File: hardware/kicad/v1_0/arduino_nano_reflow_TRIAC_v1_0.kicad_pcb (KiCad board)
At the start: 2 copper layers, 100 x 50 mm, 34 parts, among them J1 AC IN 220v, J10 CONN_01X17, J11 CONN_01X03, J12 MOUNTING_HOLE, J13 MOUNTING_HOLE, J14 MOUNTING_HOLE, J15 MOUNTING_HOLE, J2 HEATER, J3 DC IN 12V, J4 12v FAN, J5 CONN_01X03, J6 CONN_01X03, J7 CONN_01X03, J8 CONN_01X03, J9 CONN_01X05, Q1 IRF540N, U1 MOC3020M

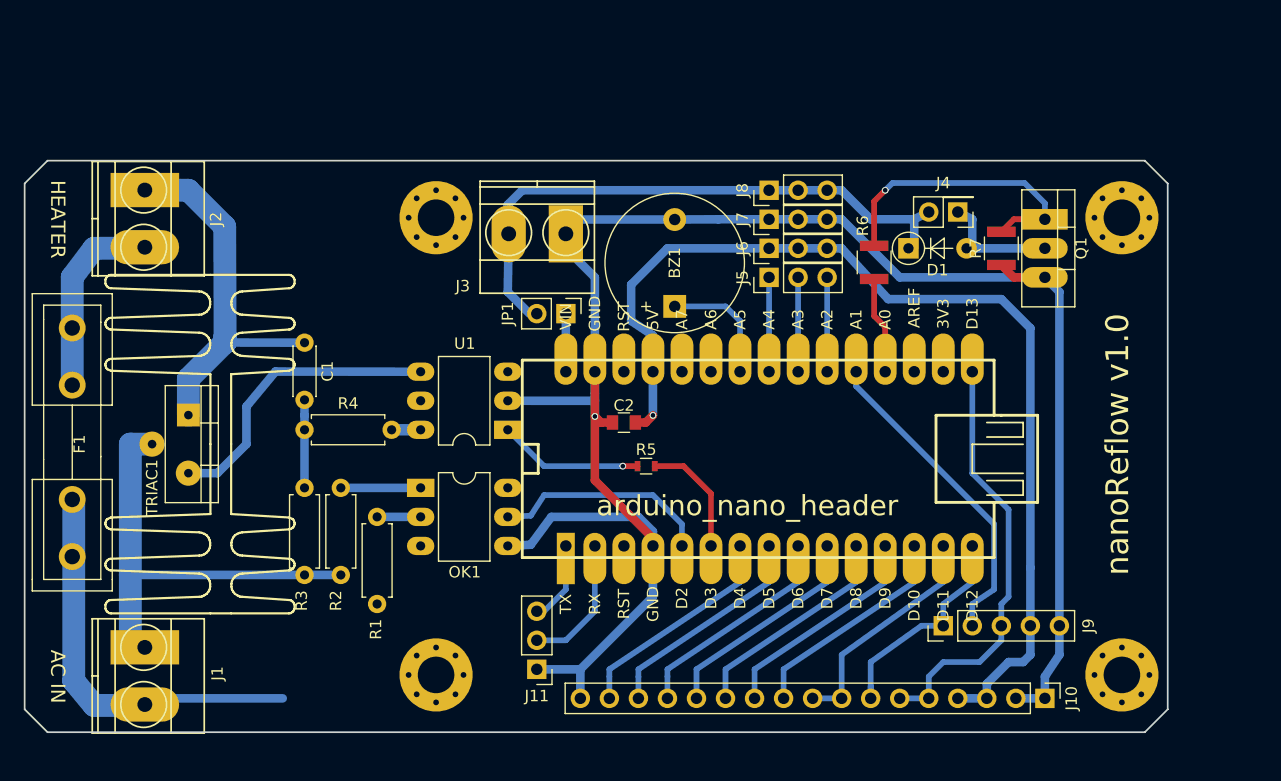
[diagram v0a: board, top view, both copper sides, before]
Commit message: - new revision of board - suitable for production with oshpark - updated footprints - cross checked with original schematics
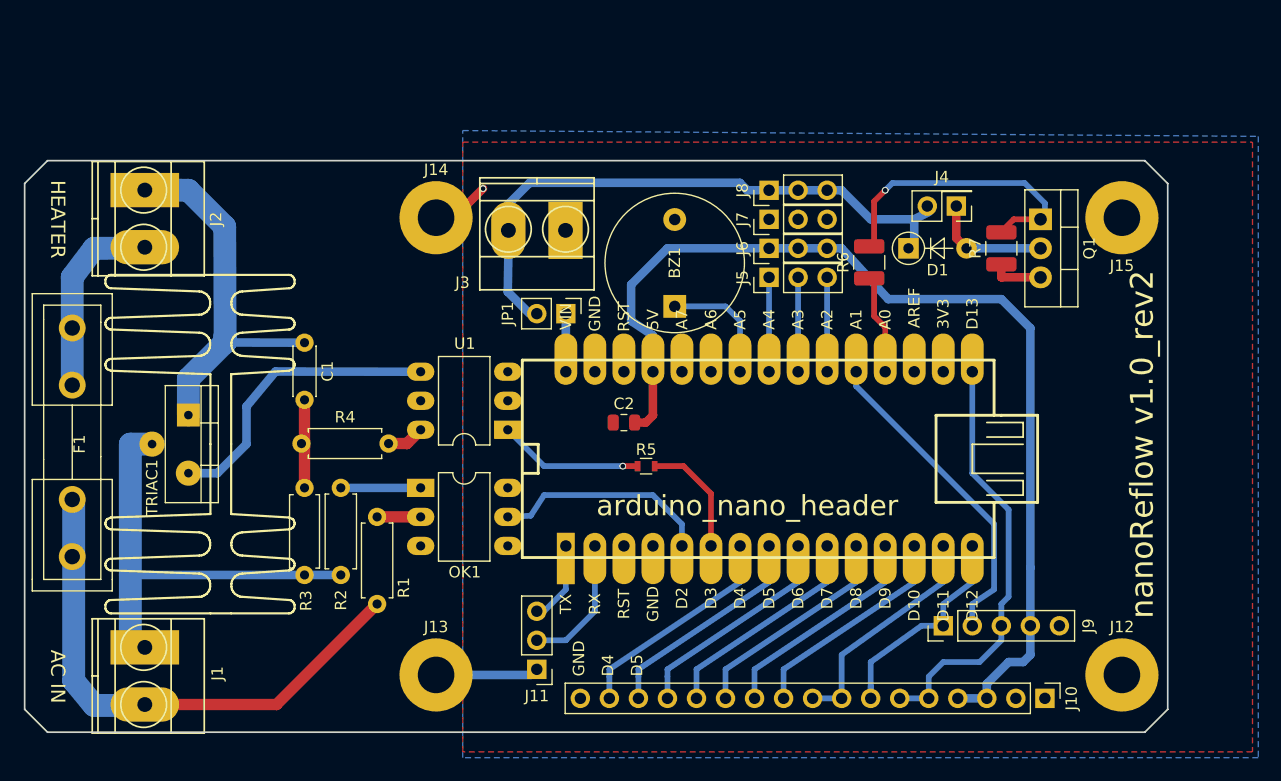
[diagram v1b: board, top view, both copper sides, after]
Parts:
- BZ1: footprint Buzzers_Beepers:Buzzer_12x9.5RM7.6 -> Buzzer_Beeper:Buzzer_12x9.5RM7.6
- C2: footprint Capacitors_SMD:C_0805 -> Capacitor_SMD:C_0805_2012Metric
- J12, J13, J14, J15: footprint Mounting_Holes:MountingHole_3.2mm_M3_Pad_Via -> MountingHole:MountingHole_3.2mm_M3_Pad
- Q1: footprint TO_SOT_Packages_THT:TO-220_Vertical -> Package_TO_SOT_THT:TO-220-3_Vertical
- R1, R2: footprint Resistors_THT:R_Axial_DIN0207_L6.3mm_D2.5mm_P7.62mm_Horizontal -> Resistor_THT:R_Axial_DIN0207_L6.3mm_D2.5mm_P7.62mm_Horizontal
- R6, R7: footprint Resistors_SMD:R_1210 -> Resistor_SMD:R_1210_3225Metric
- moved R4 1.23 mm to (124.7, 92.7)
- moved J4 0.54 mm to (182.0, 72.0)
- moved R6 0.43 mm to (174.4, 76.9)
- moved Q1 0.38 mm to (189.4, 73.1)
- moved J3 0.30 mm to (147.8, 74.1)
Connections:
- J12 pad 1: Net-(J12-Pad1) -> GND
- J13 pad 1: Net-(J13-Pad1) -> GND
- J14 pad 1: Net-(J14-Pad1) -> GND
- J15 pad 1: Net-(J15-Pad1) -> GND
- R1 pad 1: (no net) -> AC2_IN
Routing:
- net GND: track 169.1 -> 18.7 mm
- net AC2_IN: track 34.9 -> 46.7 mm
- net /AC_CAP: track 7.06 -> 7.92 mm
- net /MOC_AC1: track 2.54 -> 3.31 mm
- net /OC2: track 3.18 -> 3.81 mm
- net 12v: track 51.4 -> 51.9 mm
- net 5V: track 90.9 -> 90.8 mm, vias 1 -> 0
- added copper zone on B.Cu, net GND
- added copper zone on F.Cu, net GND
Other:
- board text added: "D4"
- board text added: "D5"
- board text added: "GND"
- board text added: "nanoReflow v1.0_rev2"
- board text removed: "nanoReflow v1.0"

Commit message: update footprint to match kicad 5.1.6 - SIP suitable for oshpark
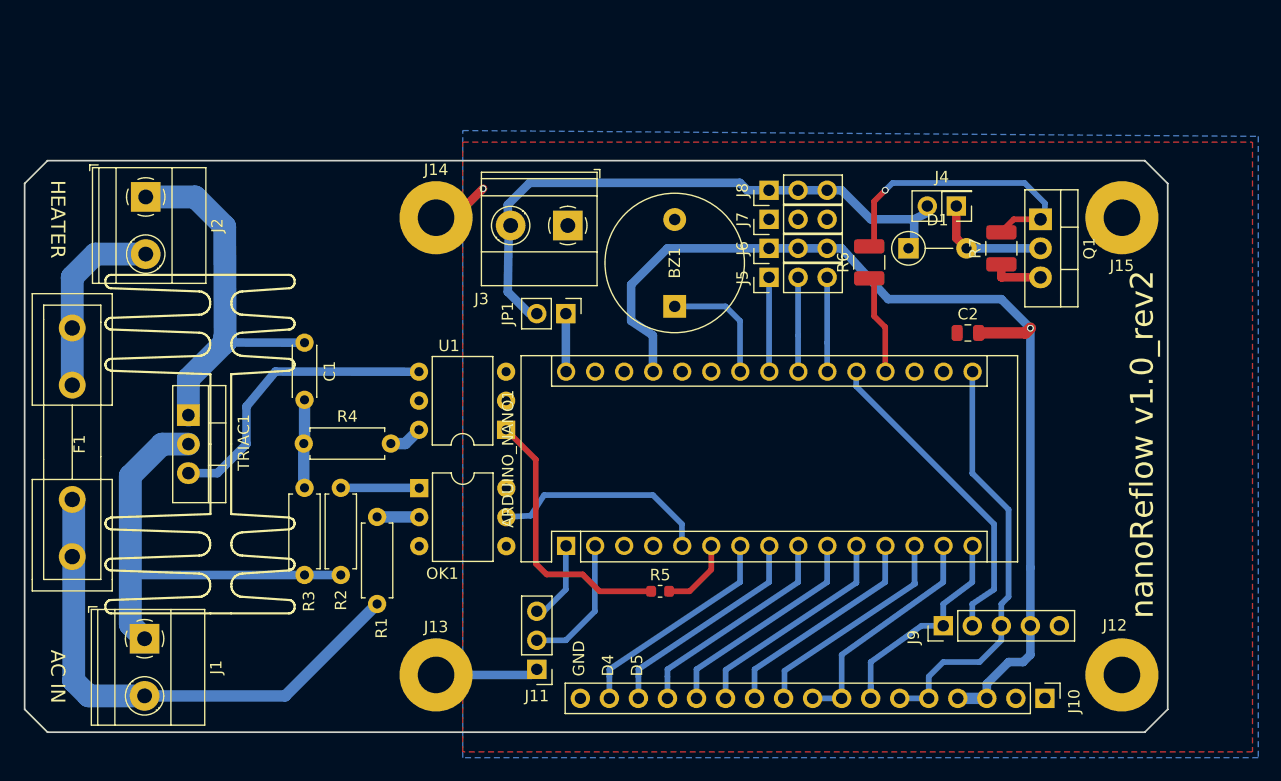
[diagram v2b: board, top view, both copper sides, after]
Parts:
- ARDUINO_NANO1: footprint local_modules:arduino_nano_header -> Module:Arduino_Nano
- C1: footprint Capacitors_THT:C_Disc_D4.3mm_W1.9mm_P5.00mm -> Capacitor_THT:C_Disc_D4.3mm_W1.9mm_P5.00mm
- D1: footprint Diodes_THT:D_A-405_P5.08mm_Vertical_AnodeUp -> Diode_THT:D_A-405_P5.08mm_Vertical_AnodeUp
- J1, J2, J3: footprint Connectors_Terminal_Blocks:TerminalBlock_Pheonix_MKDS1.5-2pol -> TerminalBlock_Phoenix:TerminalBlock_Phoenix_MKDS-1,5-2_1x02_P5.00mm_Horizontal
- J10: footprint Pin_Headers:Pin_Header_Straight_1x17_Pitch2.54mm -> Connector_PinHeader_2.54mm:PinHeader_1x17_P2.54mm_Vertical
- J9: footprint Pin_Headers:Pin_Header_Straight_1x05_Pitch2.54mm -> Connector_PinHeader_2.54mm:PinHeader_1x05_P2.54mm_Vertical
- OK1, U1: footprint Housings_DIP:DIP-6_W7.62mm_LongPads -> Package_DIP:DIP-6_W7.62mm
- R3, R4: footprint Resistors_THT:R_Axial_DIN0207_L6.3mm_D2.5mm_P7.62mm_Horizontal -> Resistor_THT:R_Axial_DIN0207_L6.3mm_D2.5mm_P7.62mm_Horizontal
- R5: footprint Resistors_SMD:R_0603 -> Resistor_SMD:R_0603_1608Metric
- TRIAC1: footprint local_modules:TO-220_Vertical_BT137 -> Package_TO_SOT_THT:TO-220-3_Vertical
- moved C2 31.1 mm to (183.0, 83.1)
- moved ARDUINO_NANO1 20.5 mm to (147.9, 101.7), turned to 90 degrees
- moved R5 11.0 mm to (156.1, 105.7)
- moved J1 0.76 mm to (111.0, 109.8)
- moved J2 0.61 mm to (111.1, 71.2)
- moved J3 0.47 mm to (148.0, 73.7)
- moved R4 0.20 mm to (124.9, 92.7)
- moved U1 0.15 mm to (142.6, 91.5)
- moved OK1 0.13 mm to (135.0, 96.6)
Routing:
- net Net-(R5-Pad1): track 12.7 -> 23.9 mm, vias 1 -> 0
- net /DIMM_CTRL: track 10.5 -> 6.55 mm
- net /FAN_CTRL: track 11.7 -> 8.52 mm
- net AC1_IN: track 37.6 -> 39.4 mm
- net 5V: track 90.8 -> 89.8 mm, vias 0 -> 1
- net AC2_IN: track 46.7 -> 45.9 mm
- net /AC_CAP: track 7.92 -> 8.51 mm

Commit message: updated PCB to v1.0_rev3 - more space for connectors and rewired for better access to FAN port
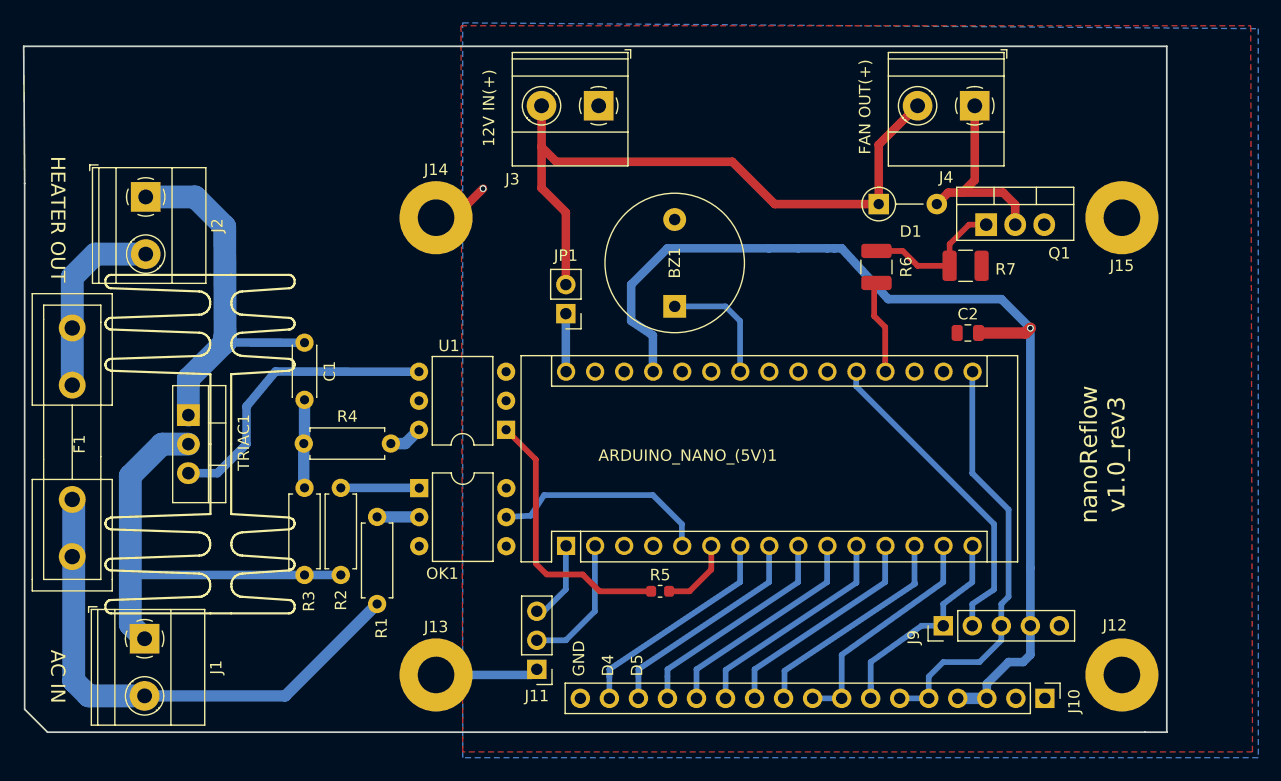
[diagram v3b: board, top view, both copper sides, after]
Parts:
- removed J5, J6, J7, J8: CONN_01X03, Pin_Headers:Pin_Header_Straight_1x03_Pitch2.54mm
- BZ1: value Buzzer -> Buzzer with generator
- J4: value 12v FAN -> 12V FAN; footprint Pin_Headers:Pin_Header_Straight_2x01_Pitch2.54mm -> TerminalBlock_Phoenix:TerminalBlock_Phoenix_MKDS-1,5-2_1x02_P5.00mm_Horizontal
- moved J3 10.8 mm to (150.7, 63.2)
- moved J4 8.92 mm to (183.6, 63.2)
- moved Q1 4.78 mm to (184.6, 73.6), turned to 0 degrees
- moved D1 4.66 mm to (175.2, 71.8)
- moved R7 3.48 mm to (182.8, 77.2), turned to 180 degrees
- moved R6 0.75 mm to (175.0, 77.3)
- turned JP1 to 180 degrees
- renumbered ARDUINO_NANO1 to ARDUINO_NANO_(5V)1
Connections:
- ARDUINO_NANO_(5V)1 pad 21: /A2 -> (no net)
- ARDUINO_NANO_(5V)1 pad 22: /A3 -> (no net)
- ARDUINO_NANO_(5V)1 pad 23: /A4 -> (no net)
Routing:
- net Net-(Q1-Pad1): track 27.4 -> 12.7 mm, vias 1 -> 0
- net /A4: track 8.26 -> 0.00 mm
- net /A3: track 8.26 -> 0.00 mm
- net /A2: track 8.26 -> 0.00 mm
- net /FAN_GND: track 10.5 -> 17.5 mm
- net 12v: track 51.9 -> 58.1 mm
- net GND: track 18.7 -> 14.2 mm
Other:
- board size 100 x 50 mm -> 100 x 60 mm
- board text added: "12V IN(+)"
- board text added: "FAN OUT(+)"
- board text added: "HEATER OUT"
- board text added: "nanoReflow v1.0_rev3"
- board text removed: "HEATER"
- board text removed: "nanoReflow v1.0_rev2"

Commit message: add missing heatsink footprint
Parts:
- KK1: footprint local_modules:TO_220_heatsink -> local_libraries:TO_220_heatsink

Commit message: update - poslane do vyroby
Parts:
- removed J10: CONN_01X17, Connector_PinHeader_2.54mm:PinHeader_1x17_P2.54mm_Vertical
- removed J15: MOUNTING_HOLE, MountingHole:MountingHole_3.2mm_M3_Pad
- added C3: 100n, Capacitor_SMD:C_0805_2012Metric, F.Cu at (190.8, 80.2)
- added J5: CONN_01X04, Connector_PinHeader_2.54mm:PinHeader_1x04_P2.54mm_Vertical, F.Cu at (152.2, 108.7)
- added J6: K-thermocouple, TerminalBlock_Phoenix:TerminalBlock_Phoenix_MKDS-1,5-2_1x02_P5.00mm_Horizontal, F.Cu at (195.0, 63.2)
- added U2: MAX6675, Package_SO:SO-8_3.9x4.9mm_P1.27mm, F.Cu at (195.0, 85.2)
- J9: value CONN_01X05 -> MAX6675
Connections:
- ARDUINO_NANO_(5V)1 pad 10: /SD_CS -> (no net)
- ARDUINO_NANO_(5V)1 pad 11: /LCD_RESET -> (no net)
- ARDUINO_NANO_(5V)1 pad 12: /LCD_DC -> (no net)
- ARDUINO_NANO_(5V)1 pad 13: /LCD_CS -> (no net)
- ARDUINO_NANO_(5V)1 pad 14: /MOSI -> (no net)
- ARDUINO_NANO_(5V)1 pad 7: /D4 -> /SEGMENT_DIO
- ARDUINO_NANO_(5V)1 pad 8: /D5 -> /SEGMENT_CLK
- ARDUINO_NANO_(5V)1 pad 9: /D6 -> (no net)
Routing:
- net 5V: track 89.8 -> 126.3 mm
- net /TC_CS: track 28.2 -> 55.6 mm
- net /MOSI: track 20.4 -> 0.00 mm
- net Net-(J6-Pad1): track 0.00 -> 19.7 mm
- net /LCD_CS: track 19.5 -> 0.00 mm
- net /LCD_RESET: track 19.5 -> 0.00 mm
- net /SD_CS: track 19.5 -> 0.00 mm
- net /LCD_DC: track 19.5 -> 0.00 mm
- net /D5: track 19.5 -> 0.00 mm
- net /D4: track 19.5 -> 0.00 mm
- net /D6: track 19.5 -> 0.00 mm
- net /MISO: track 19.9 -> 29.4 mm
- net /SEGMENT_DIO: track 0.00 -> 9.09 mm
- net /SEGMENT_CLK: track 0.00 -> 9.09 mm
- net GND: track 14.2 -> 19.0 mm
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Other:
- rule pad_to_mask_clearance: 0.2 -> 0
- board text added: "K-Thermo (+)"
- board text added: "MISO TC_CS SCK 5V GND"
- board text added: "TM1637 Display"
- board text removed: "D4"
- board text removed: "D5"
- board text removed: "GND"
